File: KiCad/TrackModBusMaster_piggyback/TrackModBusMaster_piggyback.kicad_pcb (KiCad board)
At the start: 2 copper layers, 61 parts, among them J1 Conn_02x08_Top_Bottom, J2 Conn_02x05_Odd_Even, J3 Conn_02x08_Top_Bottom, J4 Conn_01x08, J5 Conn_01x08, Q1 BVSS123LT1G, U1 ST485EBDR, U2 ST485EBDR, U3 ST485EBDR, U4 ST485EBDR, U5 ST485EBDR, U6 PIC16F18854-SO

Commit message: updated TrackModBusMaster_piggyback
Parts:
- R7, R8, R9: moved to B.Cu
- moved R12 59.8 mm to (134.1, 109.7)
- moved R13 58.8 mm to (108.7, 58.7), turned to 270 degrees
- moved C12 52.0 mm to (108.7, 66.3), turned to 270 degrees
- moved C13 48.1 mm to (122.7, 71.1)
- moved U5 43.2 mm to (130.8, 93.7)
- moved C11 43.2 mm to (132.1, 89.7)
- moved C9 43.2 mm to (132.1, 87.1)
- moved R11 43.2 mm to (132.1, 84.6)
- moved R9 42.2 mm to (141.5, 81.3), turned to 270 degrees
- moved R8 41.8 mm to (140.0, 85.5), turned to 180 degrees
- moved R21 41.0 mm to (125.7, 55.4), turned to 180 degrees
- moved R7 38.6 mm to (138.9, 81.3), turned to 90 degrees
- moved C10 36.6 mm to (129.0, 104.1)
- moved C8 36.6 mm to (129.0, 101.6)
- moved R10 36.6 mm to (129.0, 99.1)
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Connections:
- J1 pad 13: +3V3 -> +3.3VP
- J1 pad 15: +3V3 -> +3.3VP
- J2 pad 1: Reset_A -> Rx_A
- J2 pad 10: GND -> Reset_B
- J2 pad 2: Reset_B -> Rx_B
- J2 pad 5: Rx_A -> GND
- J2 pad 6: Rx_B -> GND
- J2 pad 9: GND -> Reset_A
- J3 pad 2: Net-(J3-Pad2) -> +3V3
- R7 pad 2: Net-(R7-Pad2) -> +5V
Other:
- board outline added: 40 x 75 mm

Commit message: Finished TrackModBusMaster_piggyback
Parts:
- moved R11 17.0 mm to (118.5, 94.7), turned to 90 degrees
- moved R13 16.0 mm to (122.9, 66.0), turned to 180 degrees
- moved C12 14.4 mm to (122.9, 68.6), turned to 0 degrees
- moved C11 12.3 mm to (120.9, 94.7), turned to 270 degrees
- moved R19 12.1 mm to (137.4, 55.9), turned to 180 degrees
- moved C9 11.6 mm to (123.3, 94.7), turned to 270 degrees
- moved R20 11.2 mm to (132.1, 55.9), turned to 180 degrees
- moved R26 10.9 mm to (121.4, 55.9), turned to 180 degrees
- moved C5 6.65 mm to (134.0, 65.2)
- moved C2 6.64 mm to (134.0, 67.7)
- moved U2 6.54 mm to (133.3, 71.9)
- moved R5 6.49 mm to (132.6, 77.5)
- moved R7 6.29 mm to (134.6, 85.9), turned to 180 degrees
- moved J4 6.17 mm to (128.1, 89.3)
- moved R25 5.70 mm to (108.1, 93.5), turned to 0 degrees
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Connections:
- J3 pad 3: Net-(J3-Pad3) -> GND
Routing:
- net GND: track 0.00 -> 226.5 mm, vias 0 -> 9
- net +5V: track 0.00 -> 195.6 mm, vias 0 -> 5
- net Reset: track 0.00 -> 41.2 mm
- net SDI: track 0.00 -> 34.7 mm
- net SDO: track 0.00 -> 31.1 mm
- net SS1: track 0.00 -> 29.4 mm
- net SCK1: track 0.00 -> 29.1 mm
- net Reset_B: track 0.00 -> 28.0 mm
- net Net-(C11-Pad1): track 0.00 -> 24.6 mm
- net Reset_A: track 0.00 -> 23.9 mm
- net Rx_B: track 0.00 -> 23.6 mm, vias 0 -> 1
- net Tx_A: track 0.00 -> 20.8 mm
- net Rx_A: track 0.00 -> 20.7 mm, vias 0 -> 1
- net Tx_En: track 0.00 -> 20.5 mm
- net Net-(C10-Pad1): track 0.00 -> 19.5 mm, vias 0 -> 2
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- added copper zone on B.Cu, net GND
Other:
- board size 40 x 75 mm -> 40 x 77 mm
- board text added: "."
- board text added: ">"
- board text added: "ERR"
- board text added: "JSIF 2018"
- board text added: "ModBus/SPI Master"
- board text added: "RUN"
- board text added: "RX"
- board text added: "TX"
- board text added: "WAR"

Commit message: added elco
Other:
- outline, holes or cut-outs redrawn

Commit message: update on schematic and pcb
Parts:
- added C19: 100u, Capacitor_THT:CP_Radial_D6.3mm_P2.50mm, F.Cu at (109.0, 38.4)
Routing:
- net +5V: track 195.6 -> 192.5 mm
- net GND: track 226.5 -> 227.5 mm

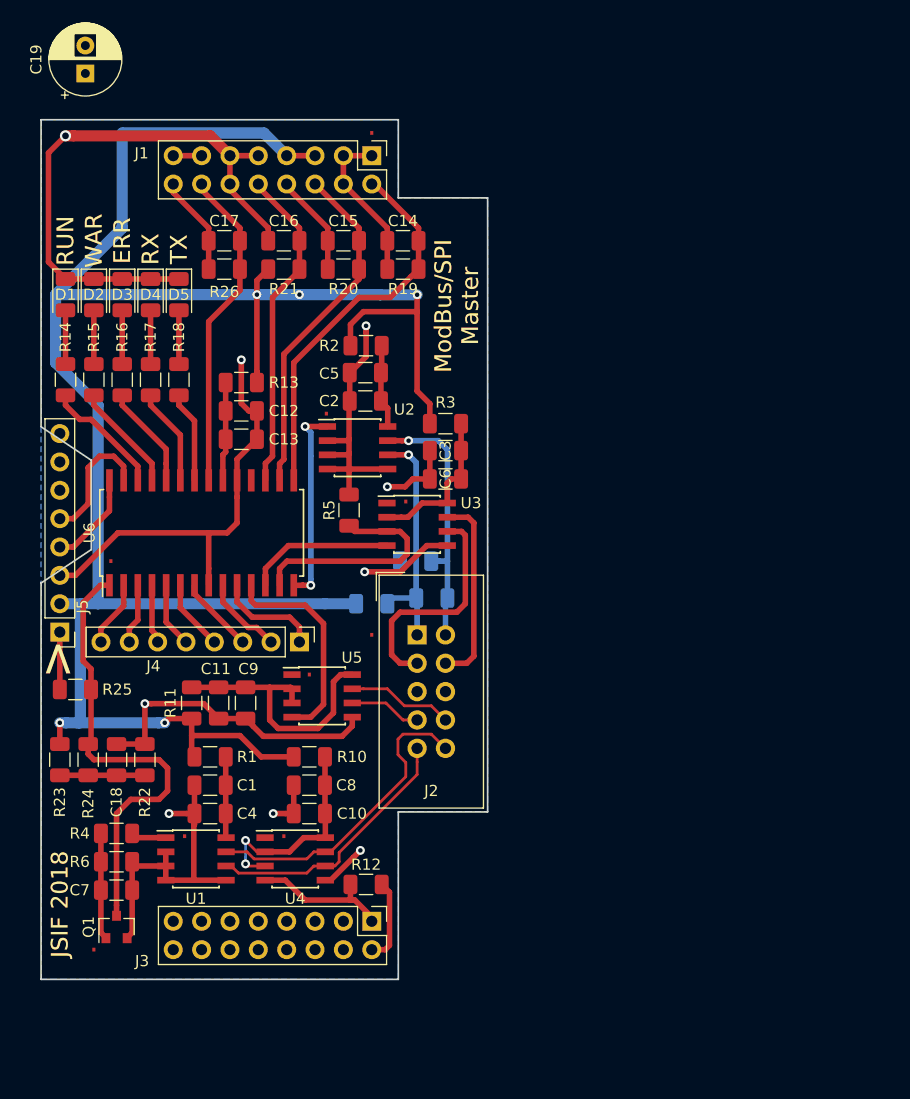
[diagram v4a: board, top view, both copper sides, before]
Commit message: updated pcb w.r.t. elco.
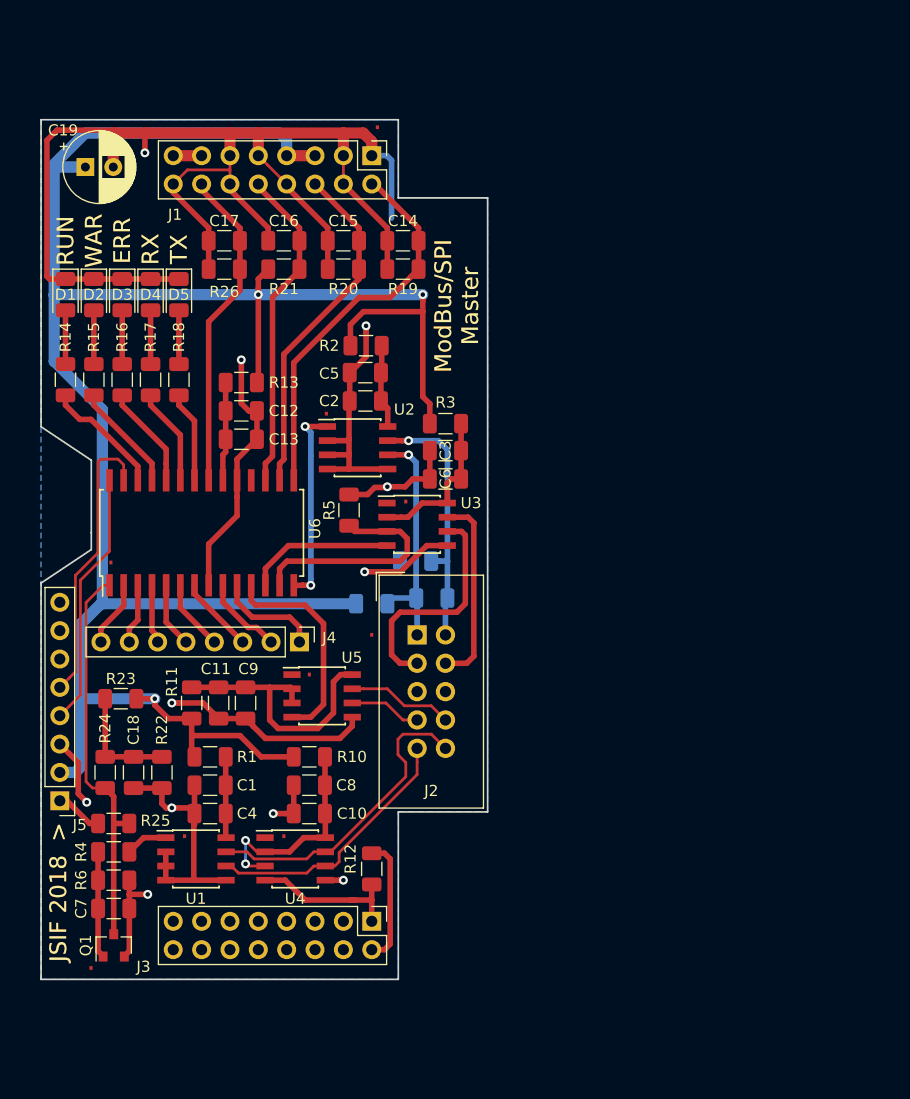
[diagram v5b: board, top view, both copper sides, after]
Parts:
- moved J5 15.1 mm to (106.7, 103.5)
- moved R25 12.5 mm to (111.5, 105.5)
- moved C19 8.38 mm to (109.0, 46.7), turned to 0 degrees
- moved R23 7.72 mm to (112.1, 94.4), turned to 180 degrees
- moved C18 1.91 mm to (113.3, 101.0), turned to 270 degrees
- moved R22 1.91 mm to (115.8, 101.0), turned to 270 degrees
- moved R24 1.91 mm to (110.7, 101.0), turned to 90 degrees
- moved R6 1.67 mm to (111.5, 110.6)
- moved C7 1.67 mm to (111.5, 113.2)
- moved Q1 1.67 mm to (111.5, 116.5)
- moved R4 1.67 mm to (111.5, 108.1)
- moved R12 1.49 mm to (134.6, 109.6), turned to 90 degrees
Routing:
- net GND: track 227.5 -> 250.1 mm, vias 9 -> 11
- net ICSPDAT: track 8.52 -> 22.9 mm
- net ICSPCLK: track 11.6 -> 25.6 mm
- net +5V: track 192.5 -> 201.0 mm, vias 5 -> 3
- net Reset: track 41.2 -> 35.5 mm
- net +3V3: track 7.49 -> 11.3 mm
- net Net-(C18-Pad1): track 7.62 -> 10.3 mm
- net Reset_Out: track 13.1 -> 14.4 mm
- net Net-(R4-Pad2): track 3.17 -> 4.33 mm
- net Vpp: track 5.14 -> 4.27 mm

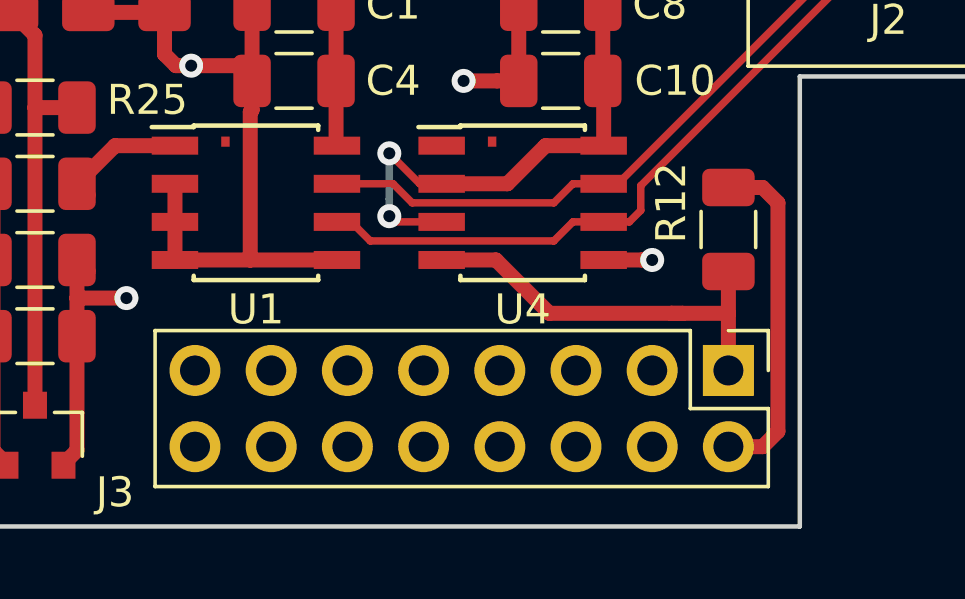
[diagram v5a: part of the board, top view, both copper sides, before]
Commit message: updated pcb according to motherboard (EthernetTarget)
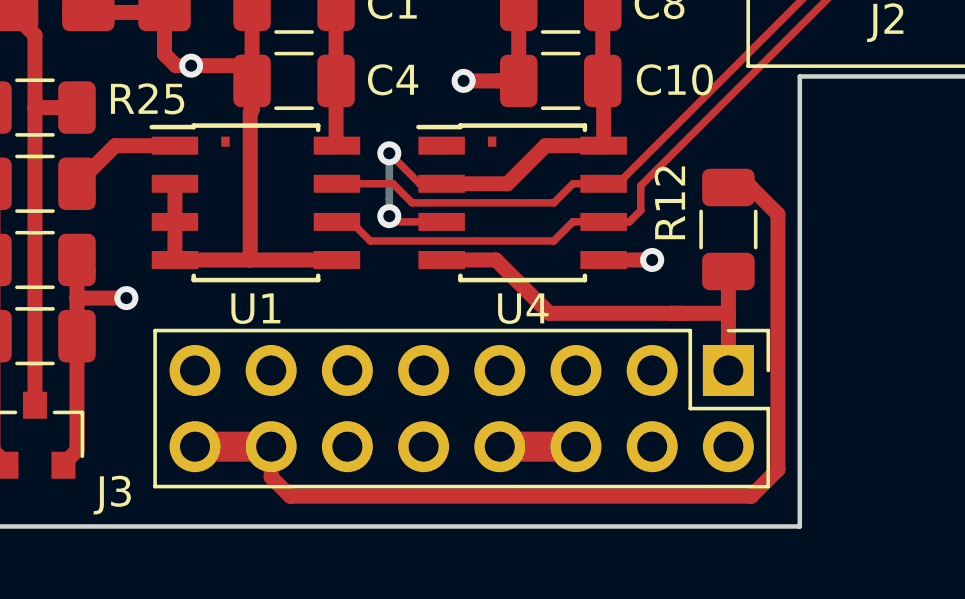
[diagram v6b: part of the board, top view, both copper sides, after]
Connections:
- J3 pad 10: Net-(J3-Pad10) -> GND
- J3 pad 12: Net-(J3-Pad12) -> GND
- J3 pad 14: Net-(J3-Pad14) -> +3V3
- J3 pad 16: Net-(J3-Pad16) -> +3V3
- J3 pad 2: +3V3 -> GND
- J3 pad 3: GND -> Net-(J3-Pad3)
- J3 pad 4: Net-(J3-Pad4) -> GND
- J3 pad 6: Net-(J3-Pad6) -> +5VP
- J3 pad 8: Net-(J3-Pad8) -> +5VP
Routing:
- net +3V3: track 11.3 -> 31.6 mm
- net +5VP: track 0.00 -> 2.54 mm

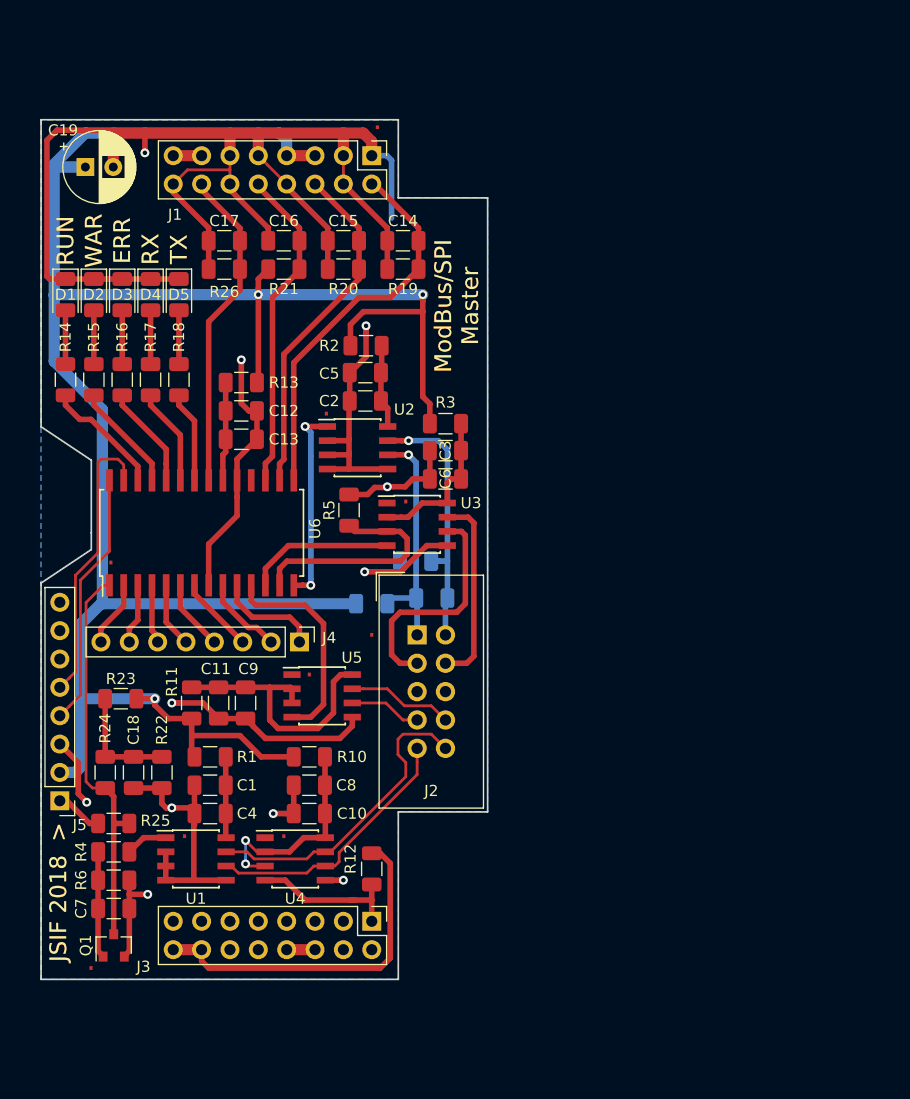
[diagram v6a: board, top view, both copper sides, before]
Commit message: Updated TrackModBusMaster_piggyback.sch and layout. completed component list to generate BOM.
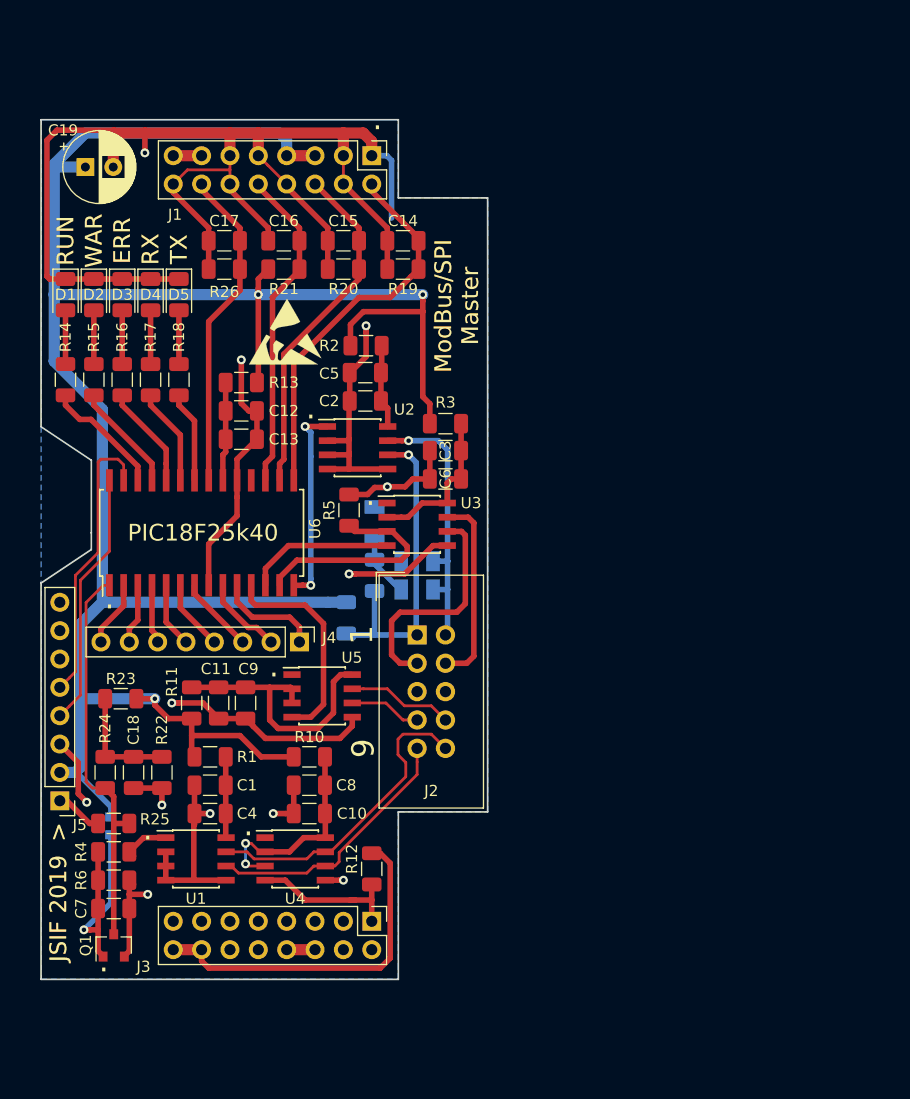
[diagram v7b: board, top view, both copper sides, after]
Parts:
- added C20: 100n, Capacitor_SMD:C_1206_3216Metric, B.Cu at (134.9, 78.6)
- added R27: 60E, Resistor_SMD:R_1206_3216Metric, B.Cu at (138.7, 84.6)
- added R28: NP, Resistor_SMD:R_0603_1608Metric, B.Cu at (111.3, 105.8)
- added REF**: ESD-Logo_6.6x6mm_SilkScreen, Symbol:ESD-Logo_6.6x6mm_SilkScreen, F.Cu at (126.9, 61.5)
- C1, C12, C18, C2, C3, C8, C9: value 2.2u -> 4.7u
- C19: value 100u -> 220u
- Q1: value BVSS123LT1G -> NTR5103NT1G
- R1, R10, R11, R13, R2, R3: value 1E -> 0E
- R12, R19, R20, R21, R26, R5: value 4k7 -> 4k99
- R14, R15, R16, R17, R18: value 301E -> 300E
- R22: value 100k -> 110k
- R4: value 100E -> 1k
- R7: value 3k9 -> 1k
- R8: value 120E -> 60E
- R9: value 1k00 -> 1k
- U6: value PIC16F18854-SO -> PIC18F25K40
- moved R8 5.52 mm to (134.9, 83.3), turned to 90 degrees
- moved R7 2.62 mm to (132.3, 87.1), turned to 90 degrees
- moved R9 0.13 mm to (138.7, 82.0)
- turned R12 to 270 degrees
- turned R25 to 180 degrees
- turned R6 to 0 degrees
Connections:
- R12 pad 1: Reset_Out -> +3V3
- R12 pad 2: +3V3 -> Reset_Out
- R25 pad 1: Vpp -> Reset
- R25 pad 2: Reset -> Vpp
- R6 pad 1: GND -> Net-(C7-Pad1)
- R6 pad 2: Net-(C7-Pad1) -> GND
- R8 pad 1: Rx_B -> Rx_A
- R8 pad 2: Rx_A -> Net-(C20-Pad1)
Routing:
- net Net-(C7-Pad1): track 9.57 -> 20.3 mm, vias 0 -> 1
- net Rx_A: track 20.7 -> 28.7 mm
- net Net-(C20-Pad1): track 0.00 -> 5.58 mm
- net +5V: track 201.0 -> 205.5 mm
- net Rx_B: track 23.6 -> 25.1 mm
- net Tx_En: track 20.5 -> 19.7 mm
- net GND: track 250.1 -> 249.8 mm, vias 11 -> 12
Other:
- board text added: "1"
- board text added: "10"
- board text added: "2"
- board text added: "9"
- board text added: "JSIF 2019"
- board text added: "PIC18F25k40"
- board text removed: "JSIF 2018"

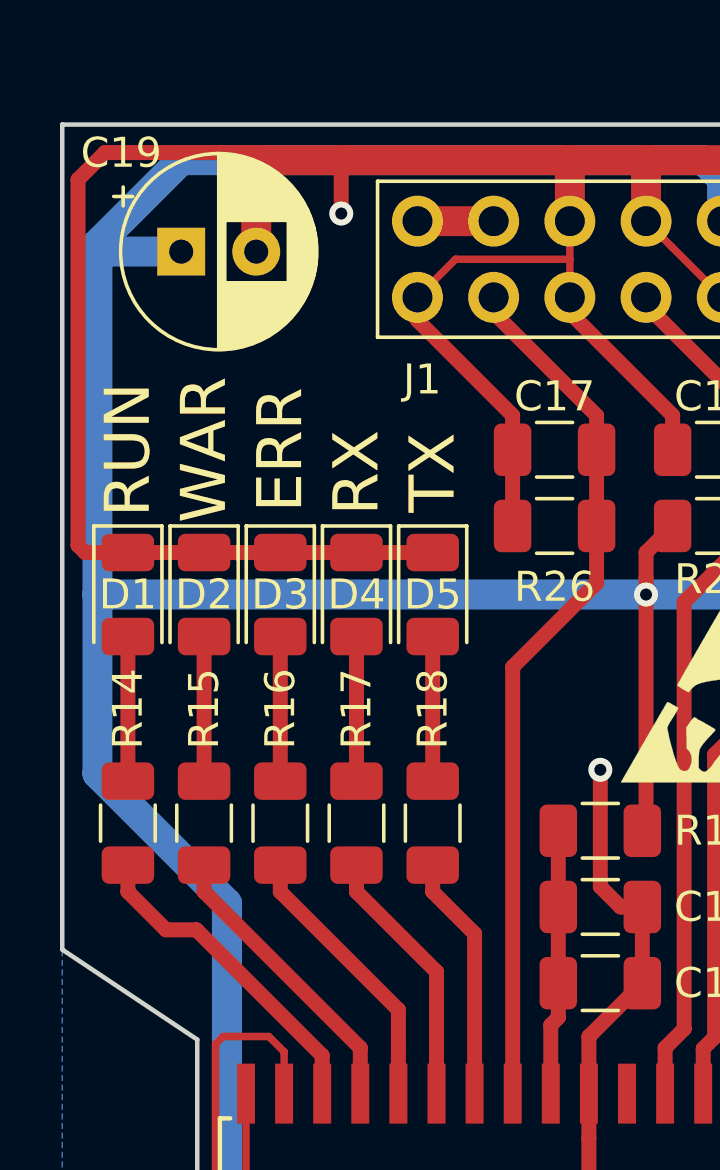
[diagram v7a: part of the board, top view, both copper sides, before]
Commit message: Updated Led's of TrackModBusMaster_piggyback.
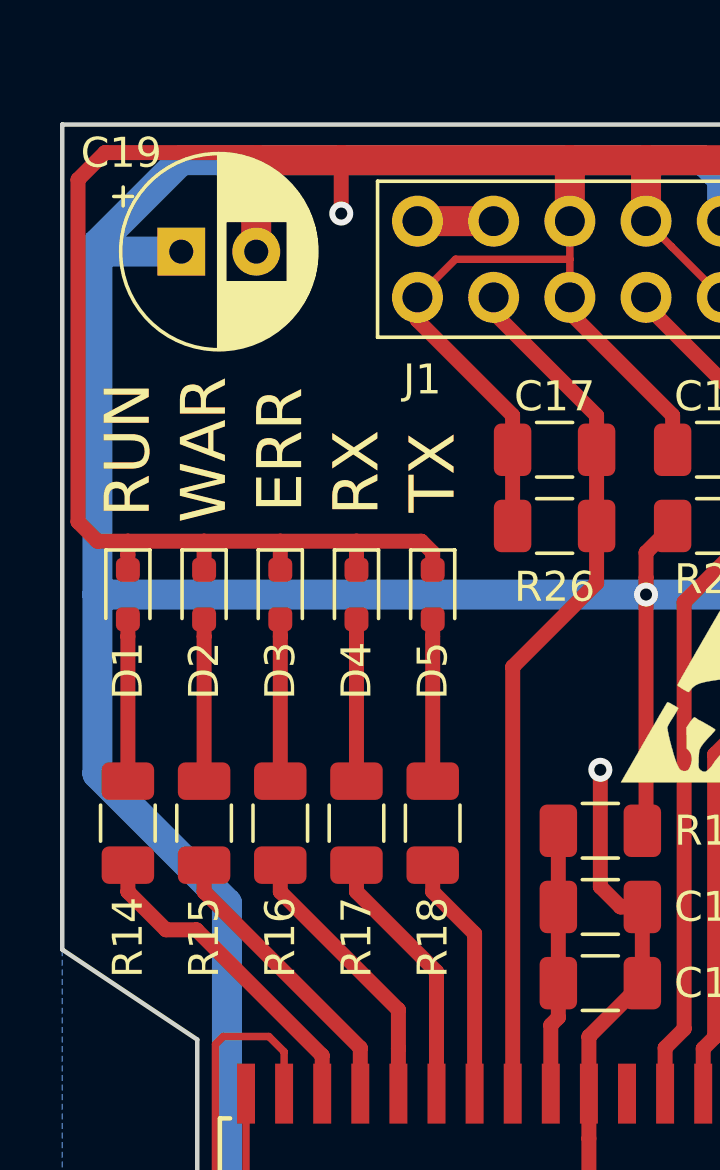
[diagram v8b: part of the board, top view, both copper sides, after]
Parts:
- D1, D2, D3, D4, D5: footprint LED_SMD:LED_1206_3216Metric -> Diode_SMD:LED_0.8x0.8
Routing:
- net GND: track 249.8 -> 253.7 mm
- net Net-(D5-Pad2): track 4.82 -> 5.39 mm
- net Net-(D4-Pad2): track 4.82 -> 5.39 mm
- net Net-(D3-Pad2): track 4.82 -> 5.39 mm
- net Net-(D2-Pad2): track 4.82 -> 5.39 mm
- net Net-(D1-Pad2): track 4.82 -> 5.39 mm
